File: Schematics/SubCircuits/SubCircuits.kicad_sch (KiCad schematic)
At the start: 0 parts

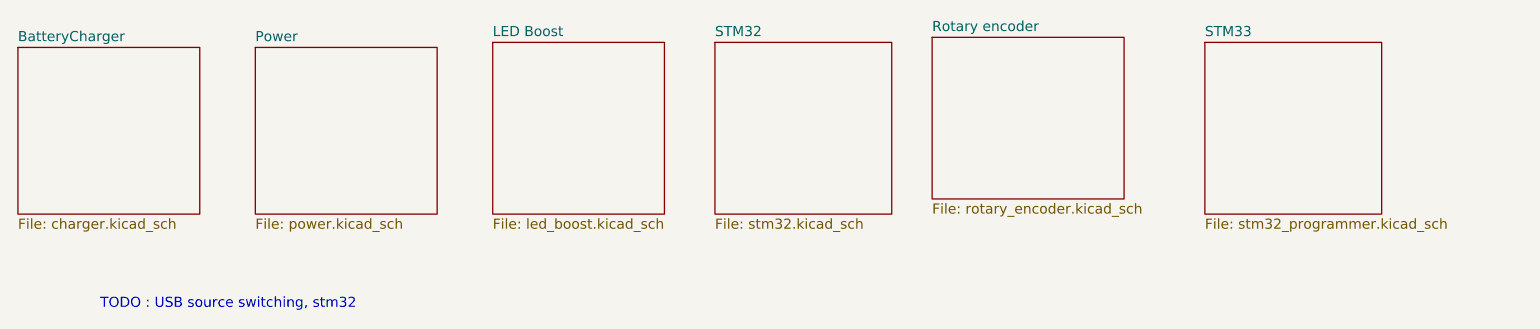
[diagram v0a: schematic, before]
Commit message: Added defunct subcircuit project
superseded by modular mainboard
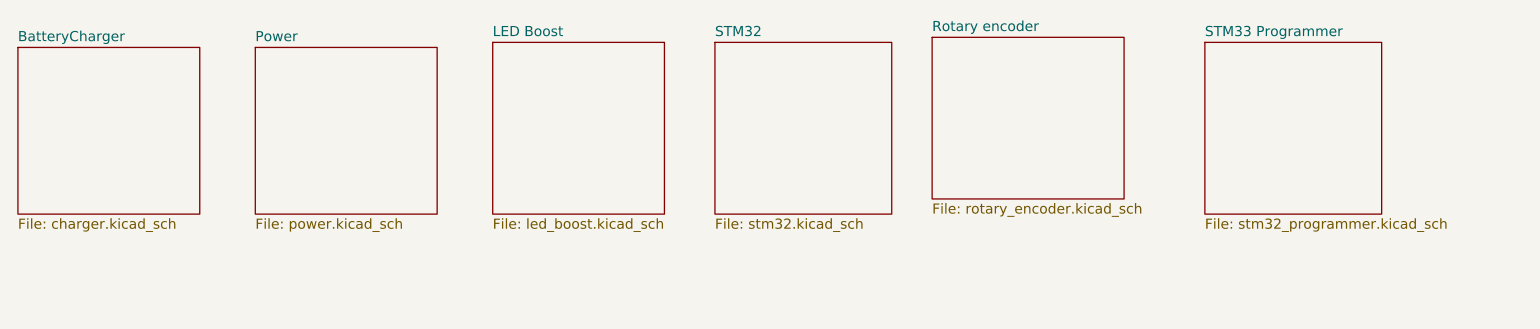
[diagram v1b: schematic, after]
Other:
- sheet STM33 renamed STM33 Programmer
- note removed: "TODO : USB source switching, stm32"
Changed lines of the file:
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@@
-(kicad_sch (version 20210126) (generator eeschema)
+(kicad_sch (version 20210406) (generator eeschema)
   (paper "A4")
-  (text "TODO : USB source switching, stm32" (at 81.28 71.12 180)
-    (effects (font (size 1.27 1.27)) (justify right bottom))
-  )
   (sheet (at 38.735 38.1) (size 22.86 20.955)
     (stroke (width 0.0006) (type solid) (color 0 0 0 0))
@@
     (stroke (width 0.0006) (type solid) (color 0 0 0 0))
     (fill (color 0 0 0 0.0000))
-    (property "Sheet name" "STM33" (id 0) (at 187.96 36.8293 0)
+    (property "Sheet name" "STM33 Programmer" (id 0) (at 187.96 36.8293 0)
       (effects (font (size 1.27 1.27)) (justify left bottom))
     )
@@
     )
     (path "/881dfa9b-c9ea-4319-a14f-5c7ca1d25c28/c69d57d6-3665-4b13-a4bf-517c21cb1694"
-      (reference "R5") (unit 1) (value "TBD") (footprint "Resistor_SMD:R_0603_1608Metric")
+      (reference "R5") (unit 1) (value "0") (footprint "Resistor_SMD:R_0603_1608Metric")
     )
     (path "/881dfa9b-c9ea-4319-a14f-5c7ca1d25c28/49761eef-a6df-458f-beb4-f61e7a61e239"
@@
       (reference "#PWR0132") (unit 1) (value "GND") (footprint "")
     )
+    (path "/e33ec2bc-4d72-418b-b961-758c9bd9db6e/8460e5dd-ee2c-4ad8-b50a-9cc39a7cbad7"
+      (reference "#PWR0136") (unit 1) (value "VBUS") (footprint "")
+    )
+    (path "/e33ec2bc-4d72-418b-b961-758c9bd9db6e/e6806fc1-0fbb-4db1-aa6a-4100a3378101"
+      (reference "#PWR0137") (unit 1) (value "GND") (footprint "")
+    )
     (path "/e33ec2bc-4d72-418b-b961-758c9bd9db6e/1d5090dd-1650-45bf-913b-70aada87f7a6"
       (reference "C6") (unit 1) (value "10u") (footprint "Capacitor_SMD:C_0603_1608Metric")
@@
       (reference "C9") (unit 1) (value "10u") (footprint "Capacitor_SMD:C_0603_1608Metric")
     )
+    (path "/e33ec2bc-4d72-418b-b961-758c9bd9db6e/56e251c5-8737-48ab-a42e-3b5a4e01bf22"
+      (reference "D2") (unit 1) (value "SS24") (footprint "Diode_SMD:D_SMA")
+    )
     (path "/e33ec2bc-4d72-418b-b961-758c9bd9db6e/58a4a3d3-d119-478a-8fb4-25983cc79b55"
       (reference "J4") (unit 1) (value "Batt_alt") (footprint "Connector_JST:JST_PH_S2B-PH-K_1x02_P2.00mm_Horizontal")
@@
       (reference "L2") (unit 1) (value "2.2u") (footprint "Inductor_SMD:L_Coilcraft_XxL4040")
     )
+    (path "/e33ec2bc-4d72-418b-b961-758c9bd9db6e/7556f78d-3efb-4f20-ab74-fd2ee23d22bb"
+      (reference "Q1") (unit 1) (value "AO3401A") (footprint "Package_TO_SOT_SMD:SOT-23")
+    )
     (path "/e33ec2bc-4d72-418b-b961-758c9bd9db6e/9a2ba64b-3e43-4e18-81aa-41df1edfa487"
       (reference "R6") (unit 1) (value "100") (footprint "Resistor_SMD:R_0603_1608Metric")
     )
+    (path "/e33ec2bc-4d72-418b-b961-758c9bd9db6e/bc518aad-7107-469e-9c09-6e5c24500dc9"
+      (reference "R10") (unit 1) (value "100k") (footprint "Resistor_SMD:R_0603_1608Metric")
+    )
     (path "/e33ec2bc-4d72-418b-b961-758c9bd9db6e/973055df-16e0-4474-8b3c-4475418f157d"
       (reference "SW1") (unit 1) (value "PHB2UOATS1A") (footprint "PHB2UOATS1A:PHB2UOATS1A")
@@
       (reference "U2") (unit 1) (value "TPS63001") (footprint "Package_SON:Texas_DRC0010J_ThermalVias")
     )
-    (path "/6fb210cf-9b45-4512-97e9-3e551817fa95/c4fe3a3a-e52f-433d-96f1-93ce2212084f"
-      (reference "#PWR0124") (unit 1) (value "+3.3V") (footprint "")
-    )
-    (path "/6fb210cf-9b45-4512-97e9-3e551817fa95/8470cb41-e970-409a-b363-b13a94fc43f5"
-      (reference "#PWR0126") (unit 1) (value "GND") (footprint "")
-    )
-    (path "/6fb210cf-9b45-4512-97e9-3e551817fa95/6f50b091-69e6-4203-bac8-0e5f37c035b6"
-      (reference "#PWR0135") (unit 1) (value "GND") (footprint "")
-    )
     (path "/6fb210cf-9b45-4512-97e9-3e551817fa95/8cd624ac-cf2d-424f-ae99-0e37c0fa752b"
       (reference "D3") (unit 1) (value "WS2812B") (footprint "custom:WS2812B_2020")
@@
     )
     (path "/aaec8030-a288-47a6-9ca4-a07ff5da0374/b4f744dc-0bde-4e99-9650-3fc509dac48c"
-      (reference "C16") (unit 1) (value "100n") (footprint "Capacitor_SMD:C_0603_1608Metric")
+      (reference "C16") (unit 1) (value "0.1u") (footprint "Capacitor_SMD:C_0603_1608Metric")
     )
     (path "/aaec8030-a288-47a6-9ca4-a07ff5da0374/552b2762-377e-4f2b-9697-dc4213cb2053"
-      (reference "J7") (unit 1) (value "I") (footprint "Connector_PinHeader_2.54mm:PinHeader_1x04_P2.54mm_Vertical")
+      (reference "J7") (unit 1) (value "Input") (footprint "Connector_PinHeader_2.54mm:PinHeader_1x04_P2.54mm_Vertical")
     )
     (path "/aaec8030-a288-47a6-9ca4-a07ff5da0374/2af91d5b-05cd-4fbb-8b4b-cdee7ddfd187"
@@
     )
     (path "/aaec8030-a288-47a6-9ca4-a07ff5da0374/434d0b60-304b-4b1b-b72b-cf7f3956166e"
-      (reference "J11") (unit 1) (value "O") (footprint "Connector_PinHeader_2.54mm:PinHeader_1x04_P2.54mm_Vertical")
+      (reference "J11") (unit 1) (value "Output") (footprint "Connector_PinHeader_2.54mm:PinHeader_1x04_P2.54mm_Vertical")
     )
     (path "/aaec8030-a288-47a6-9ca4-a07ff5da0374/9ef1dedd-8c1c-4516-b90b-70ad974a20f2"
@@
       (reference "U5") (unit 1) (value "STM32G070K") (footprint "Package_QFP:LQFP-32_7x7mm_P0.8mm")
     )
+    (path "/980a7306-e072-4f5c-8aeb-f920fb926fbd/96b08add-8e55-45c1-85a5-840a0a744cf5"
+      (reference "#PWR0125") (unit 1) (value "GND") (footprint "")
+    )
+    (path "/980a7306-e072-4f5c-8aeb-f920fb926fbd/cca8bea7-1486-403d-9bbb-cae263ed6964"
+      (reference "#PWR0127") (unit 1) (value "+3.3V") (footprint "")
+    )
+    (path "/980a7306-e072-4f5c-8aeb-f920fb926fbd/9b0ceff8-e8cc-4e38-b174-bdb127e420dd"
+      (reference "#PWR0128") (unit 1) (value "GND") (footprint "")
+    )
+    (path "/980a7306-e072-4f5c-8aeb-f920fb926fbd/d8e0259a-491d-42de-91f7-a9e078ed76ca"
+      (reference "#PWR0129") (unit 1) (value "+3.3V") (footprint "")
+    )
+    (path "/980a7306-e072-4f5c-8aeb-f920fb926fbd/0fdffbbe-f7f2-4cb7-973c-6f2e77dfb034"
+      (reference "#PWR0130") (unit 1) (value "+3.3V") (footprint "")
+    )
+    (path "/980a7306-e072-4f5c-8aeb-f920fb926fbd/c8871bae-aa32-45a5-bdd6-a9a81ea38e36"
+      (reference "#PWR0133") (unit 1) (value "GND") (footprint "")
+    )
+    (path "/980a7306-e072-4f5c-8aeb-f920fb926fbd/4427c44e-6141-4023-a19e-06a18bee8c81"
+      (reference "C10") (unit 1) (value "10u") (footprint "Capacitor_SMD:C_0603_1608Metric")
+    )
+    (path "/980a7306-e072-4f5c-8aeb-f920fb926fbd/a2005ba3-28cd-49ad-bb51-67c2f1c652c3"
+      (reference "J3") (unit 1) (value "Rot") (footprint "Connector_PinHeader_2.54mm:PinHeader_1x05_P2.54mm_Vertical")
+    )
+    (path "/980a7306-e072-4f5c-8aeb-f920fb926fbd/1da2b5ed-0b44-4490-8a44-1c8be6954f77"
+      (reference "R7") (unit 1) (value "47k") (footprint "Resistor_SMD:R_0603_1608Metric")
+    )
+    (path "/980a7306-e072-4f5c-8aeb-f920fb926fbd/8dbd5c59-bcc3-46fb-97ad-f4429e2efef2"
+      (reference "R8") (unit 1) (value "47k") (footprint "Resistor_SMD:R_0603_1608Metric")
+    )
+    (path "/980a7306-e072-4f5c-8aeb-f920fb926fbd/8841b6fd-b02a-4b39-8830-570dca93ad2b"
+      (reference "R9") (unit 1) (value "47k") (footprint "Resistor_SMD:R_0603_1608Metric")
+    )
+    (path "/980a7306-e072-4f5c-8aeb-f920fb926fbd/5101f623-62f6-4c5f-bae6-20fb32d81bc6"
+      (reference "SW4") (unit 1) (value "Rot") (footprint "Rotary_Encoder:RotaryEncoder_Alps_EC11E-Switch_Vertical_H20mm")
+    )
     (path "/b70baf3a-7267-4281-a2b4-579d49543506/6476168d-2c28-4458-ac80-3848d49cf79f"
